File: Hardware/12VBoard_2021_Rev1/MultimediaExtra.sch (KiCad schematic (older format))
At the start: 33 parts, among them Q1 CSD18537NQ5A, Q2 CSD18531Q5A, U7 LM5116, U8 INA198

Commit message: Redesigned low current ports schematic
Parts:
- gave numbers to parts that had none: 6
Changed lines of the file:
@@
 P 6075 1650
 AR Path="/5F74F36B/5F971CD6/5FC479FB" Ref="U?"  Part="1"
-AR Path="/5F74F36B/5F8236F9/5FC479FB" Ref="U?"  Part="1"
-F 0 "U?" H 6450 2337 60  0000 C CNN
+AR Path="/5F74F36B/5F8236F9/5FC479FB" Ref="U5"  Part="1"
+F 0 "U5" H 6450 2337 60  0000 C CNN
 F 1 "LT1910" H 6450 2231 60  0000 C CNN
 F 2 "" H 6075 1650 60  0001 C CNN
@@
 P 5800 1725
 AR Path="/5F74F36B/5F971CD6/5FC47A01" Ref="C?"  Part="1"
-AR Path="/5F74F36B/5F8236F9/5FC47A01" Ref="C?"  Part="1"
-F 0 "C?" H 5892 1771 50  0000 L CNN
+AR Path="/5F74F36B/5F8236F9/5FC47A01" Ref="C6"  Part="1"
+F 0 "C6" H 5892 1771 50  0000 L CNN
 F 1 "0.1uF" H 5892 1680 50  0000 L CNN
 F 2 "" H 5800 1725 50  0001 C CNN
@@
 P 7125 1725
 AR Path="/5F74F36B/5F971CD6/5FC47A07" Ref="C?"  Part="1"
-AR Path="/5F74F36B/5F8236F9/5FC47A07" Ref="C?"  Part="1"
-F 0 "C?" H 6950 1775 50  0000 L CNN
+AR Path="/5F74F36B/5F8236F9/5FC47A07" Ref="C7"  Part="1"
+F 0 "C7" H 6950 1775 50  0000 L CNN
 F 1 "10uF" H 6625 1675 50  0000 L CNN
 F 2 "" H 7125 1725 50  0001 C CNN
@@
 P 6475 1900
 AR Path="/5F74F36B/5F971CD6/5FC47A0D" Ref="#PWR?"  Part="1"
-AR Path="/5F74F36B/5F8236F9/5FC47A0D" Ref="#PWR?"  Part="1"
-F 0 "#PWR?" H 6475 1650 50  0001 C CNN
+AR Path="/5F74F36B/5F8236F9/5FC47A0D" Ref="#PWR05"  Part="1"
+F 0 "#PWR05" H 6475 1650 50  0001 C CNN
 F 1 "GND" H 6480 1727 50  0000 C CNN
 F 2 "" H 6475 1900 50  0001 C CNN
@@
 P 7400 1575
 AR Path="/5F74F36B/5F971CD6/5FC47A27" Ref="Q?"  Part="1"
-AR Path="/5F74F36B/5F8236F9/5FC47A27" Ref="Q?"  Part="1"
-F 0 "Q?" H 7604 1621 50  0000 L CNN
+AR Path="/5F74F36B/5F8236F9/5FC47A27" Ref="Q9"  Part="1"
+F 0 "Q9" H 7604 1621 50  0000 L CNN
 F 1 "IRLML2060" H 7604 1530 50  0000 L CNN
 F 2 "Package_TO_SOT_SMD:SOT-23" H 7600 1500 50  0001 L CIN
@@
 P 7500 1175
 AR Path="/5F74F36B/5F971CD6/5FC47A42" Ref="R?"  Part="1"
-AR Path="/5F74F36B/5F8236F9/5FC47A42" Ref="R?"  Part="1"
-F 0 "R?" H 7570 1221 50  0000 L CNN
+AR Path="/5F74F36B/5F8236F9/5FC47A42" Ref="R16"  Part="1"
+F 0 "R16" H 7570 1221 50  0000 L CNN
 F 1 "0.01" H 7570 1130 50  0000 L CNN
 F 2 "" V 7430 1175 50  0001 C CNN
@@
 P 5675 1250
 AR Path="/5F74F36B/5F971CD6/5FC47A48" Ref="R?"  Part="1"
-AR Path="/5F74F36B/5F8236F9/5FC47A48" Ref="R?"  Part="1"
-F 0 "R?" V 5468 1250 50  0000 C CNN
+AR Path="/5F74F36B/5F8236F9/5FC47A48" Ref="R15"  Part="1"
+F 0 "R15" V 5468 1250 50  0000 C CNN
 F 1 "5.1K" V 5559 1250 50  0000 C CNN
 F 2 "" V 5605 1250 50  0001 C CNN

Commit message: Layed out logic power
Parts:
- C6: footprint (none) -> Capacitor_SMD:C_0603_1608Metric_Pad1.05x0.95mm_HandSolder
- C7: footprint (none) -> Capacitor_THT:CP_Radial_D5.0mm_P2.00mm
- R15, R16: footprint (none) -> Resistor_SMD:R_0603_1608Metric_Pad1.05x0.95mm_HandSolder
- U5: footprint (none) -> Package_SO:SOIC-8-N7_3.9x4.9mm_P1.27mm
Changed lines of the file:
@@
 F 0 "U5" H 6450 2337 60  0000 C CNN
 F 1 "LT1910" H 6450 2231 60  0000 C CNN
-F 2 "" H 6075 1650 60  0001 C CNN
+F 2 "Package_SO:SOIC-8-N7_3.9x4.9mm_P1.27mm" H 6075 1650 60  0001 C CNN
 F 3 "" H 6075 1650 60  0001 C CNN
 	1    6075 1650
@@
 F 0 "C6" H 5892 1771 50  0000 L CNN
 F 1 "0.1uF" H 5892 1680 50  0000 L CNN
-F 2 "" H 5800 1725 50  0001 C CNN
+F 2 "Capacitor_SMD:C_0603_1608Metric_Pad1.05x0.95mm_HandSolder" H 5800 1725 50  0001 C CNN
 F 3 "~" H 5800 1725 50  0001 C CNN
 	1    5800 1725
@@
 F 0 "C7" H 6950 1775 50  0000 L CNN
 F 1 "10uF" H 6625 1675 50  0000 L CNN
-F 2 "" H 7125 1725 50  0001 C CNN
+F 2 "Capacitor_THT:CP_Radial_D5.0mm_P2.00mm" H 7125 1725 50  0001 C CNN
 F 3 "~" H 7125 1725 50  0001 C CNN
 	1    7125 1725
@@
 F 0 "R16" H 7570 1221 50  0000 L CNN
 F 1 "0.01" H 7570 1130 50  0000 L CNN
-F 2 "" V 7430 1175 50  0001 C CNN
+F 2 "Resistor_SMD:R_0603_1608Metric_Pad1.05x0.95mm_HandSolder" V 7430 1175 50  0001 C CNN
 F 3 "~" H 7500 1175 50  0001 C CNN
 	1    7500 1175
@@
 F 0 "R15" V 5468 1250 50  0000 C CNN
 F 1 "5.1K" V 5559 1250 50  0000 C CNN
-F 2 "" V 5605 1250 50  0001 C CNN
+F 2 "Resistor_SMD:R_0603_1608Metric_Pad1.05x0.95mm_HandSolder" V 5605 1250 50  0001 C CNN
 F 3 "~" H 5675 1250 50  0001 C CNN
 	1    5675 1250

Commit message: Started layout of bucks
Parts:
- L6: footprint Inductor_SMD:L_0603_1608Metric_Pad1.05x0.95mm_HandSolder -> MRDT_12VoltBoard:IND_SER2915L-682KL
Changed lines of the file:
@@
 F 0 "L6" V 1585 3550 50  0000 C CNN
 F 1 "6.6uH 1.5m" V 1494 3550 50  0000 C CNN
-F 2 "Inductor_SMD:L_0603_1608Metric_Pad1.05x0.95mm_HandSolder" H 1400 3550 50  0001 C CNN
+F 2 "MRDT_12VoltBoard:IND_SER2915L-682KL" H 1400 3550 50  0001 C CNN
 F 3 "~" H 1400 3550 50  0001 C CNN
 	1    1400 3550

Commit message: found Big inductors
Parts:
- L6: value 6.6uH 1.5m -> 10uH; footprint MRDT_12VoltBoard:IND_SER2915L-682KL -> Inductor_THT:L_Radial_D27.9mm_P20.07mm_Vishay_IHB-3
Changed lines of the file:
@@
 AR Path="/5F74F36B/5F8236F9/5FE4073E" Ref="L6"  Part="1"
 F 0 "L6" V 1585 3550 50  0000 C CNN
-F 1 "6.6uH 1.5m" V 1494 3550 50  0000 C CNN
-F 2 "MRDT_12VoltBoard:IND_SER2915L-682KL" H 1400 3550 50  0001 C CNN
-F 3 "~" H 1400 3550 50  0001 C CNN
+F 1 "10uH" V 1494 3550 50  0000 C CNN
+F 2 "Inductor_THT:L_Radial_D27.9mm_P20.07mm_Vishay_IHB-3" H 1400 3550 50  0001 C CNN
+F 3 "https://www.bourns.com/docs/Product-Datasheets/1130_series.pdf" H 1400 3550 50  0001 C CNN
 	1    1400 3550
 	0    -1   -1   0

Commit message: Added all logic circuits for high current
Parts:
- R14: footprint Resistor_SMD:R_2512_6332Metric_Pad1.52x3.35mm_HandSolder -> Package_TO_SOT_THT:TO-126-2_Vertical
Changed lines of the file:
@@
 F 0 "R14" V 3143 3550 50  0000 C CNN
 F 1 "50m" V 3234 3550 50  0000 C CNN
-F 2 "Resistor_SMD:R_2512_6332Metric_Pad1.52x3.35mm_HandSolder" V 3280 3550 50  0001 C CNN
+F 2 "Package_TO_SOT_THT:TO-126-2_Vertical" V 3280 3550 50  0001 C CNN
 F 3 "~" H 3350 3550 50  0001 C CNN
 	1    3350 3550

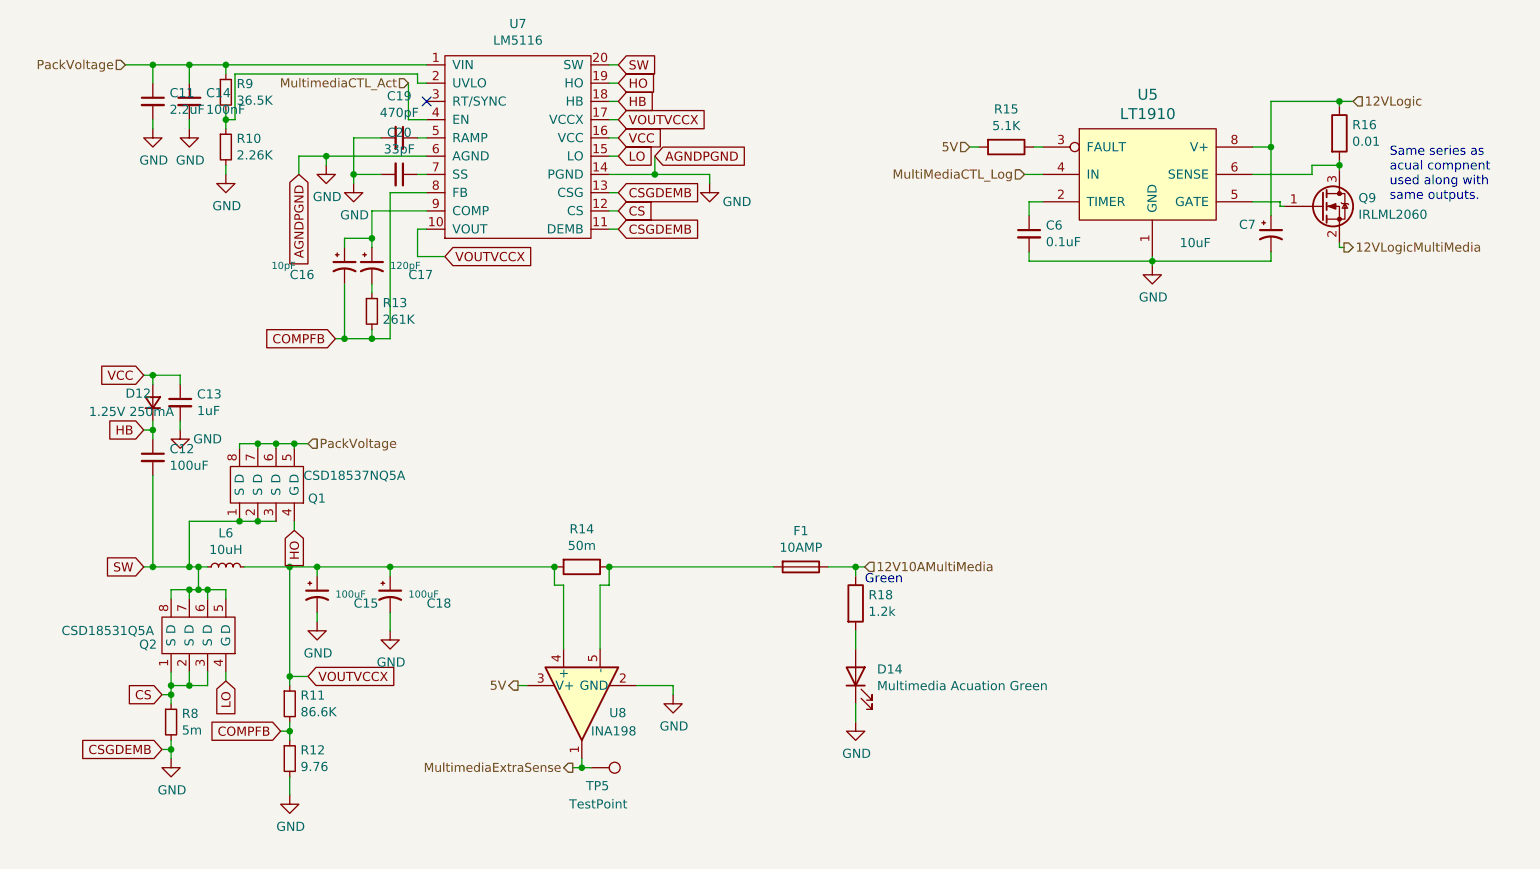
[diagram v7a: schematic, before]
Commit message: changed to big bucks
changed to the bucks used in Master due to a realization in the inductor sizing for the LM5116. It would be much bigger than previous years.
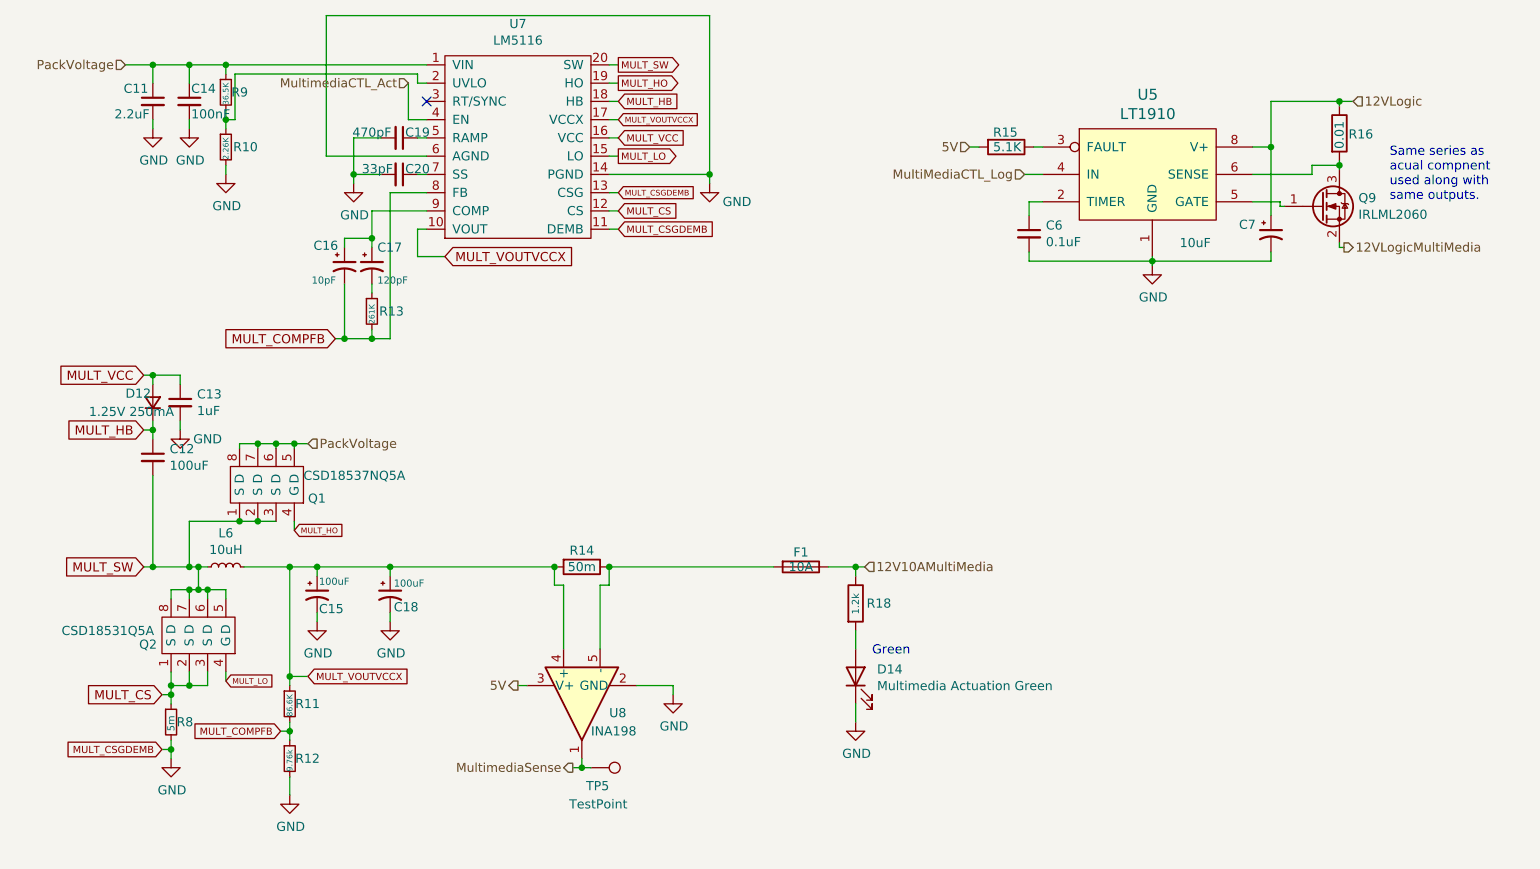
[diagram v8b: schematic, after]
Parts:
- D14: value Multimedia Acuation Green -> Multimedia Actuation Green
- F1: value 10AMP -> 10A
- R12: value 9.76 -> 9.76k
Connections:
- net COMPFB renamed MULT_COMPFB
- net CS renamed MULT_CS
- net HB renamed MULT_HB
- net HO renamed MULT_HO
- net LO renamed MULT_LO
- net MultimediaExtraSense renamed MultimediaSense
- net SW renamed MULT_SW
- net VCC renamed MULT_VCC
- net VOUTVCCX renamed MULT_VOUTVCCX
